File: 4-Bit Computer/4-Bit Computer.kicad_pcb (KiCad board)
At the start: 4 copper layers, 220.5 x 182.4 mm, 295 parts, among them J1 +12v, Q1 BC547, Q10 BC547, Q11 BC547, Q12 BC547, Q13 BC547, Q14 BC547, Q15 BC547, Q16 BC547, Q17 BC547, Q18 BC547, Q19 BC547, Q2 BC547, Q20 BC547, Q21 BC547, Q22 BC547, Q23 BC547, Q24 BC547, Q25 BC547, Q26 BC547, Q27 BC547, Q28 BC547, Q29 BC547, Q3 BC547, Q30 BC547, Q31 BC547, Q32 BC547, Q33 BC547, Q34 BC547, Q35 BC547, Q36 BC547, Q37 BC547, Q38 BC547, Q39 BC547, Q4 BC547, Q40 BC547, Q41 BC547, Q42 BC547, Q43 BC547, Q44 BC547, Q45 BC547, Q46 BC547, Q47 BC547, Q48 BC547, Q49 BC547, Q5 BC547, Q50 BC547, Q51 BC547, Q52 BC547, Q53 BC547, Q54 BC547, Q55 BC547, Q56 BC547, Q57 BC547, Q58 BC547, Q59 BC547, Q6 BC547, Q60 BC547, Q61 BC547, Q62 BC547, Q63 BC547, Q64 BC547, Q65 BC547, Q66 BC547, Q67 BC547, Q68 BC547, Q69 BC547, Q7 BC547, Q70 BC547, Q71 BC547, Q72 BC547, Q73 BC547, Q74 BC547, Q75 BC547, Q76 BC547, Q77 BC547, Q78 BC547, Q79 BC547, Q8 BC547, Q80 BC547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

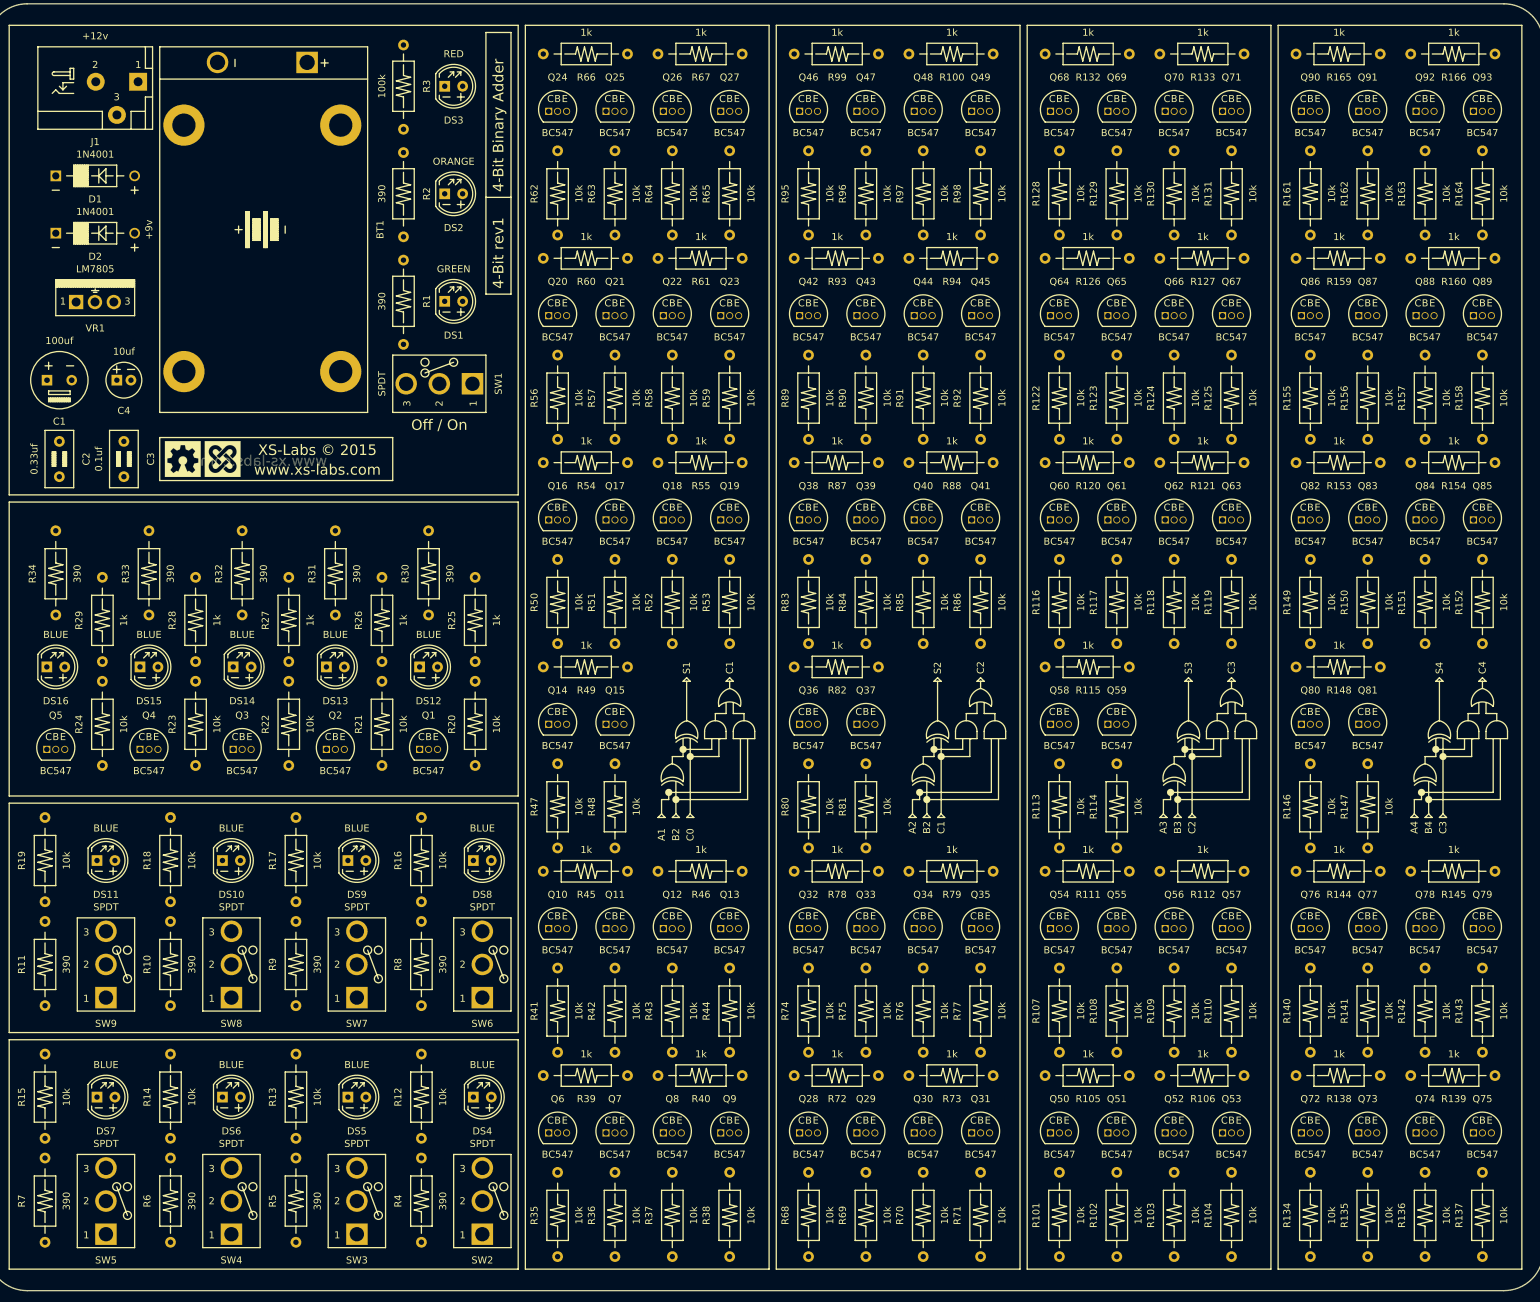
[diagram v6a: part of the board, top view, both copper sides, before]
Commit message: 4-layer routing in progress...
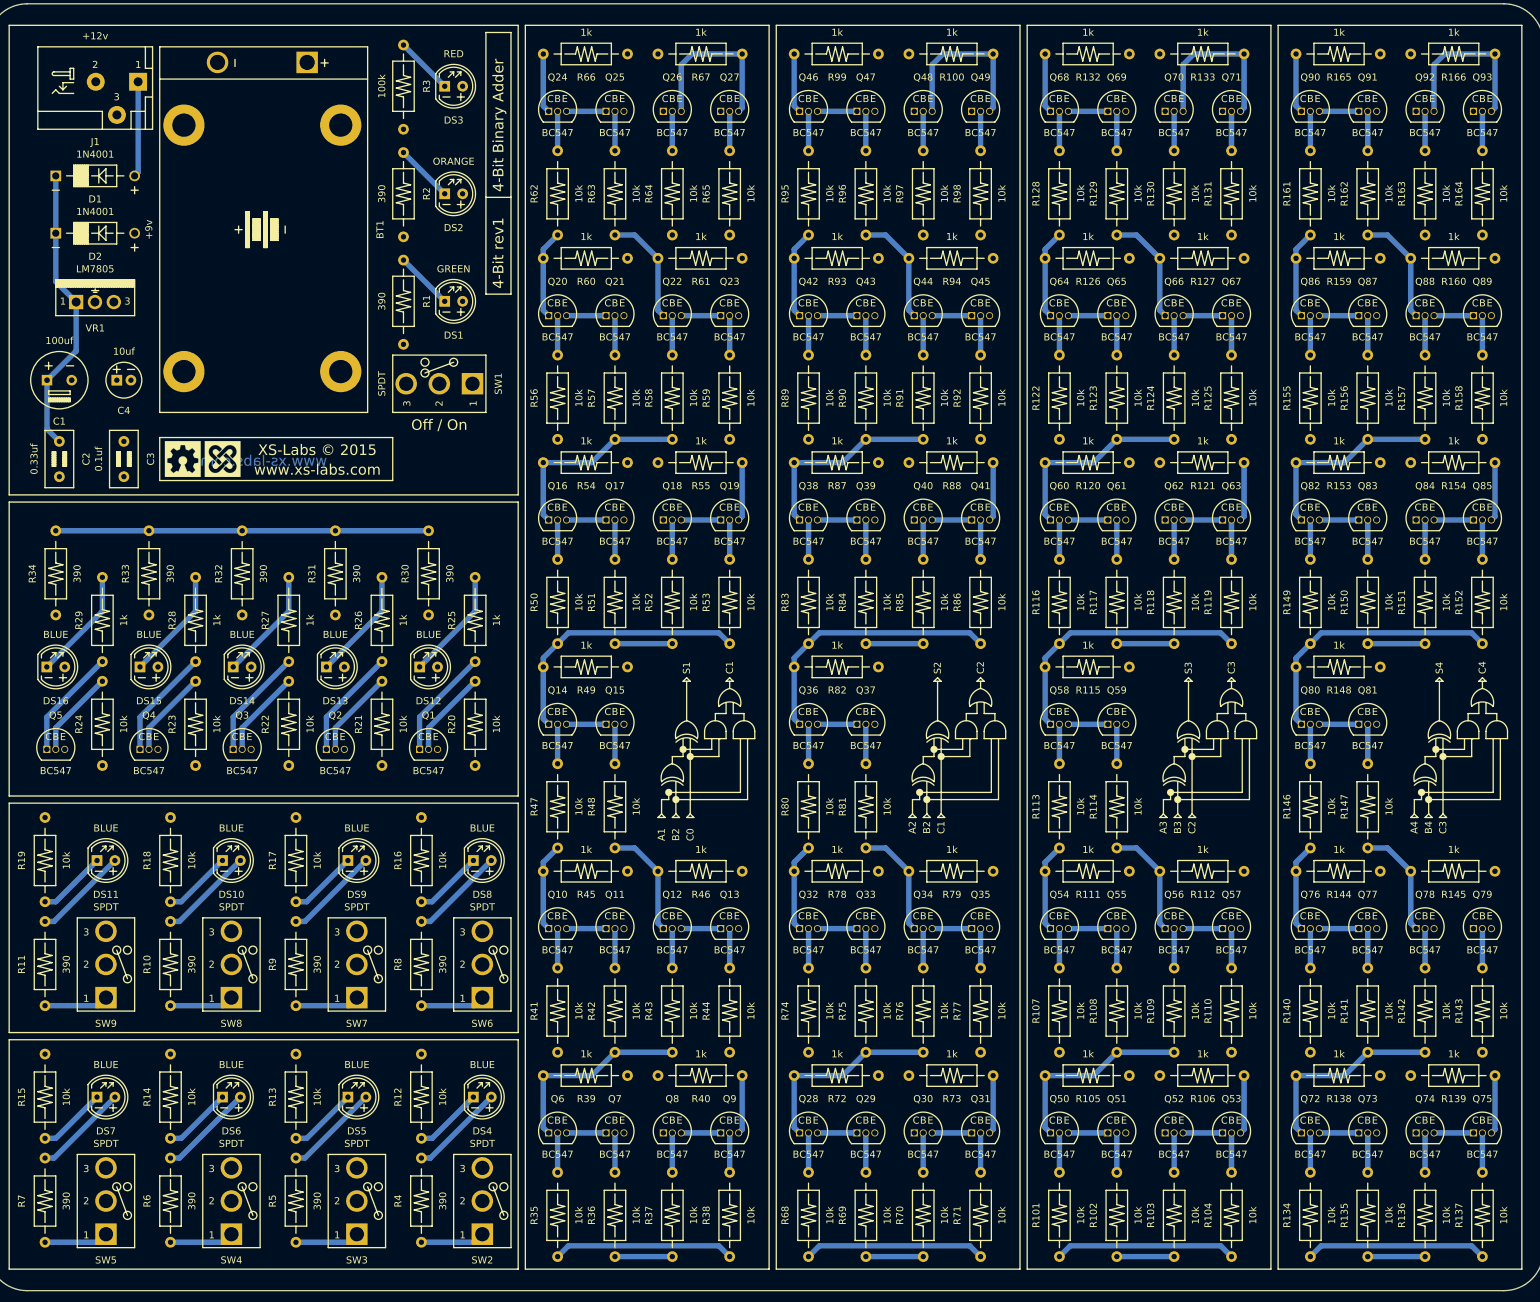
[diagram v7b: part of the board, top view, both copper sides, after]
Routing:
- net Net-(R30-Pad1): track 0.00 -> 52.8 mm
- net Net-(C1-Pad1): track 0.00 -> 41.3 mm
- net Net-(Q80-Pad1): track 0.00 -> 38.2 mm
- net Net-(Q58-Pad1): track 0.00 -> 38.2 mm
- net Net-(Q36-Pad1): track 0.00 -> 38.2 mm
- net Net-(Q14-Pad1): track 0.00 -> 38.2 mm
- net A3: track 0.00 -> 34.8 mm
- net A2: track 0.00 -> 34.8 mm
- net A4: track 0.00 -> 34.8 mm
- net A1: track 0.00 -> 34.8 mm
- net /Adder 3/C3: track 0.00 -> 32.3 mm
- net /Adder 2/C2: track 0.00 -> 32.3 mm
- net /Adder 1/C1: track 0.00 -> 32.3 mm
- net Net-(Q50-Pad1): track 0.00 -> 28.1 mm
- net Net-(Q28-Pad1): track 0.00 -> 28.1 mm
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
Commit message: Routing...
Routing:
- net Net-(R30-Pad1): track 52.8 -> 273.4 mm
- net A4: track 34.8 -> 243.8 mm
- net A3: track 34.8 -> 189.3 mm
- net A2: track 34.8 -> 134.7 mm
- net A1: track 34.8 -> 80.1 mm
- net Net-(R3-Pad1): track 0.00 -> 37.5 mm
- net Net-(BT1-Pad1): track 0.00 -> 35.7 mm
- net Net-(DS14-Pad2): track 0.00 -> 30.6 mm
- net Net-(DS16-Pad2): track 0.00 -> 30.6 mm
- net Net-(DS15-Pad2): track 0.00 -> 30.6 mm
- net Net-(DS12-Pad2): track 0.00 -> 30.6 mm
- net Net-(DS13-Pad2): track 0.00 -> 30.6 mm
- net Net-(D1-Pad2): track 13.5 -> 32.4 mm
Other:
- board size 220.5 x 182.4 mm -> 222.5 x 184.4 mm
